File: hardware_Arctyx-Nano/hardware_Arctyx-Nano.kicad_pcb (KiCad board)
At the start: 4 copper layers, 51 x 21 mm, 71 parts, among them J1 USB_C_Receptacle_USB2.0_16P, J2 Conn_01x20_Pin, J3 Conn_01x20_Pin, SW1 SW_Push, U1 ICE40UP5K-SG48ITR, U2 RP2350A-QFN60, U3 W25Q128JVP, U4 RT8075ZQW, U5 TJ-S1608SW6TDSLCCYRGB-A5, Y1 Crystal_GND24

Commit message: BOM Optimisation
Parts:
- C1, C2: value 15p -> 18p
- D1, D2, D3, D4, D5, D6: footprint LED_SMD:LED_0402_1005Metric -> LED_SMD:LED_0603_1608Metric
- moved D1 9.42 mm to (146.3, 81.9), turned to 0 degrees
- moved R16 7.17 mm to (143.9, 81.9), turned to 0 degrees
- moved D2 7.06 mm to (146.3, 80.4), turned to 0 degrees
- moved R19 5.61 mm to (138.9, 80.4), turned to 0 degrees
- moved R17 4.44 mm to (143.9, 80.4), turned to 0 degrees
- moved R18 3.51 mm to (139.0, 81.9), turned to 0 degrees
- moved D4 3.51 mm to (141.4, 80.4), turned to 0 degrees
- moved TP1 0.69 mm to (152.0, 76.6)
- moved D6 0.66 mm to (150.2, 81.5)
- moved D3 0.60 mm to (141.4, 81.9), turned to 0 degrees
- moved D5 0.51 mm to (150.2, 80.0)
- moved R20 0.37 mm to (152.7, 81.5)
- moved TP2 0.25 mm to (151.4, 74.6)
- moved R21 0.10 mm to (152.7, 80.0)
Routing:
- net 3v3: track 61.7 -> 80.6 mm, vias 21 -> 22
- net Net-(U1C-IOB_2a): track 3.38 -> 11.0 mm, vias 0 -> 2
- net Net-(U1C-IOB_0a): track 6.38 -> 10.9 mm
- net Net-(U1C-IOB_3b_G6): track 11.5 -> 7.92 mm
- net Net-(U1C-IOB_5b): track 10.1 -> 7.85 mm
- net /IO20: track 19.3 -> 20.4 mm
- net GND: track 31.8 -> 32.8 mm, vias 41 -> 40
- net /IO14: track 9.94 -> 9.20 mm
- net /IO13: track 8.15 -> 7.48 mm
- net /IO11: track 6.61 -> 7.20 mm
- net SPI_MOSI: track 11.8 -> 11.2 mm
- net /IO19: vias 0 -> 1

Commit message: Fix LED reference
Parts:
- renumbered D2 to D1, D1 to D2

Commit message: update load capacitor values
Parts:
- C1, C2: value 18p -> 15p
- R11: value 100k -> 22k
- R12: value 22k -> 100k

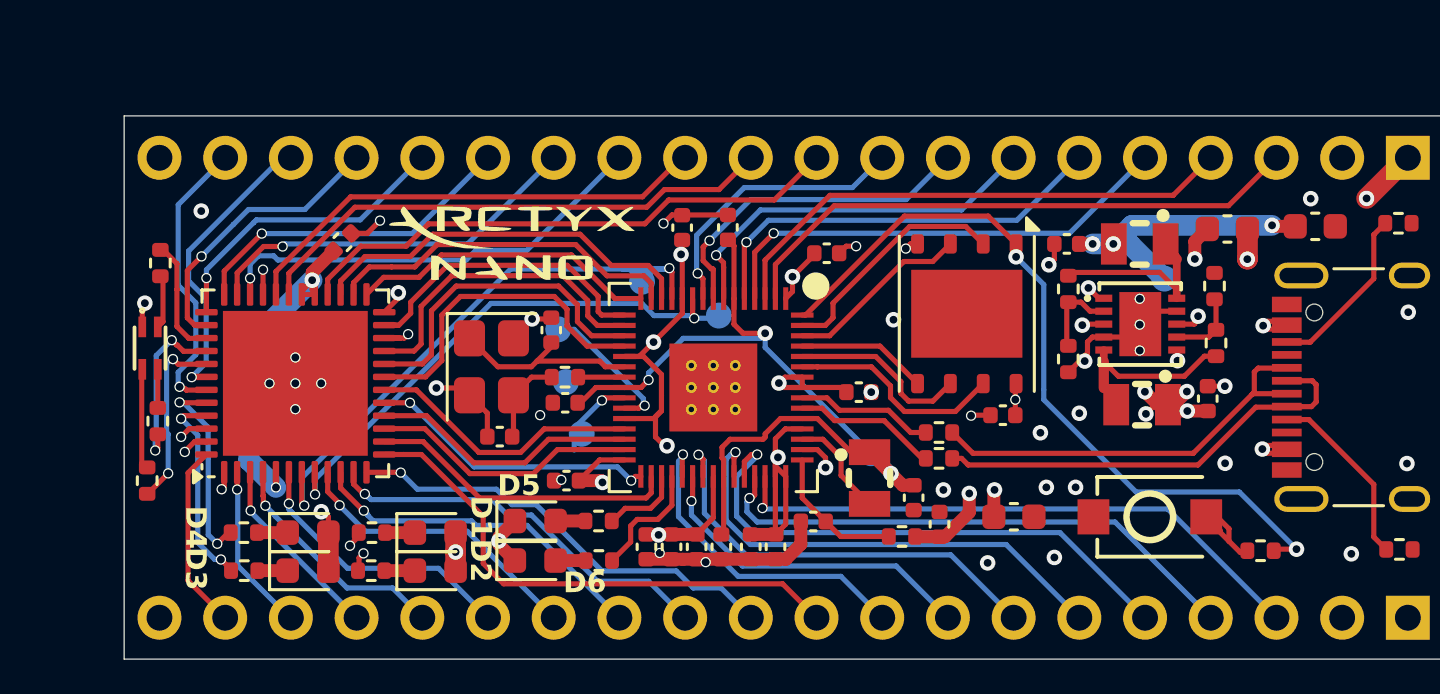
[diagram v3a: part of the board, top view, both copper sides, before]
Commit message: Removed via-in-pad
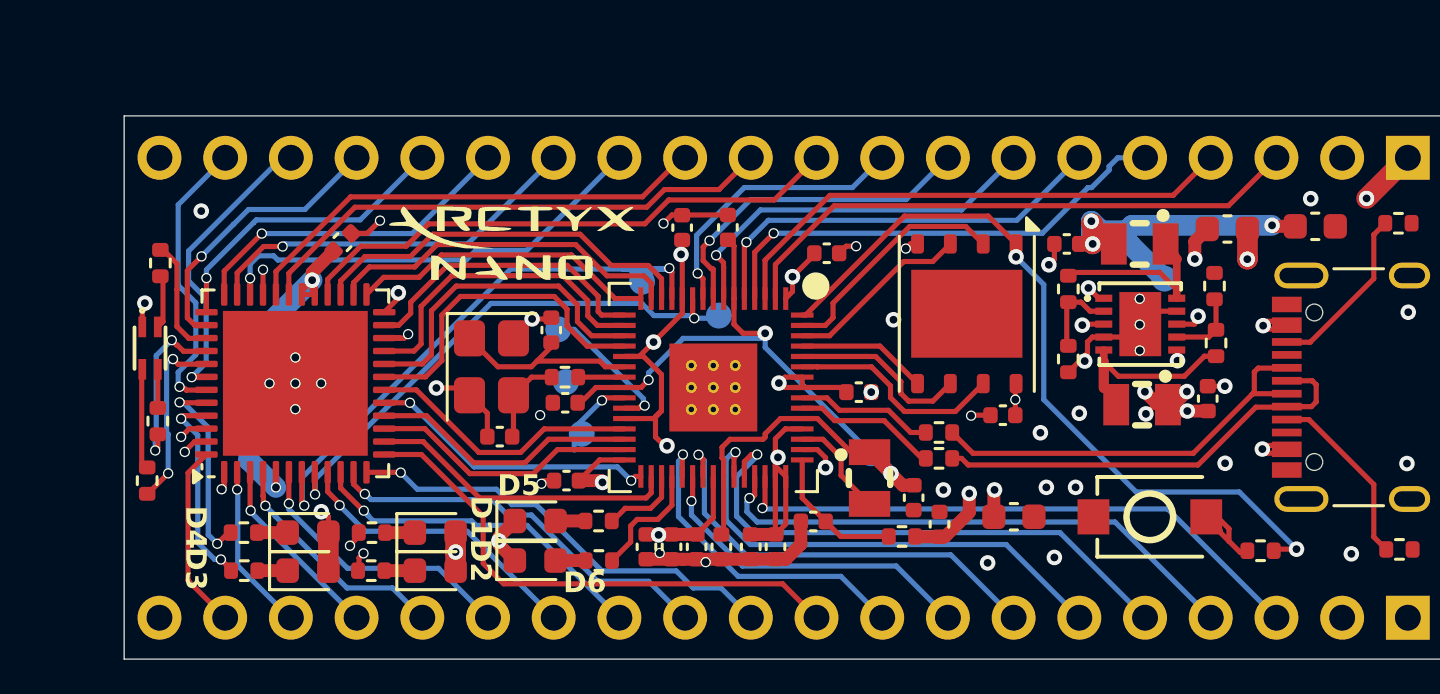
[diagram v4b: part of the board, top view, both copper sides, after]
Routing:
- net 1v2: track 68.5 -> 73.9 mm
